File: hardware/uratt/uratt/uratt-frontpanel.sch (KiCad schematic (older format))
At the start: 25 parts, among them J9 Conn_01x10, P1 TOUCH, Q3 DMP31D0U, Q4 2N7002, SW3 SW_Push (OPTION)

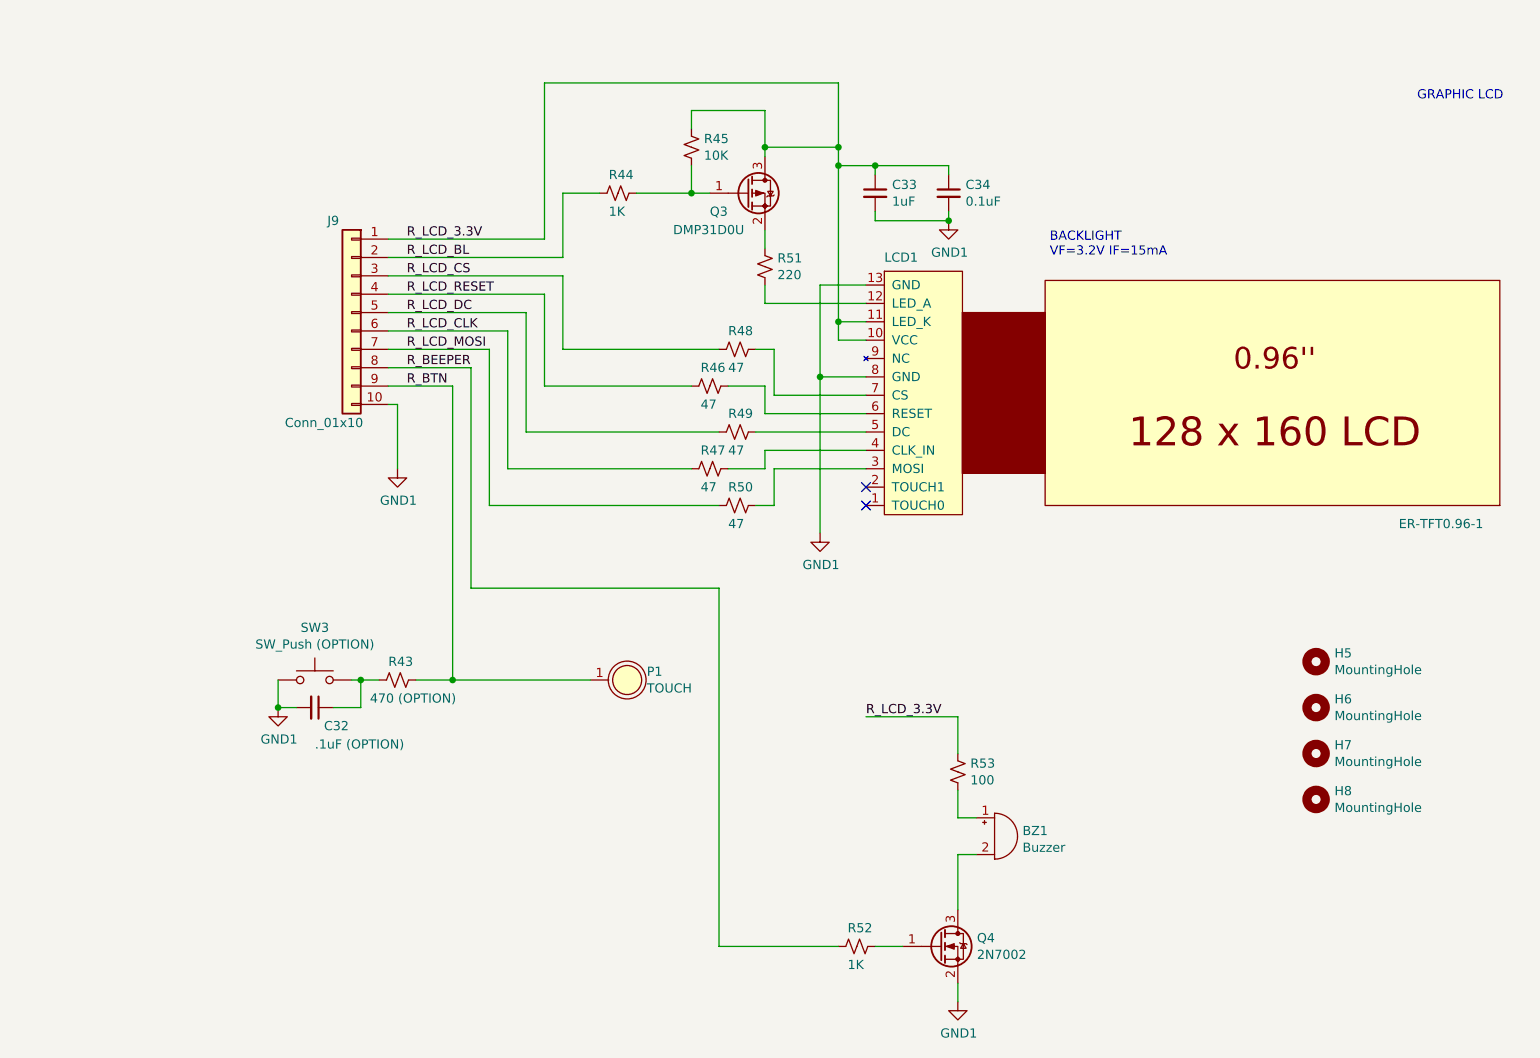
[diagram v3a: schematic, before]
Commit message: fully routed, DRC'd, outlined w/breakaways, pending final review
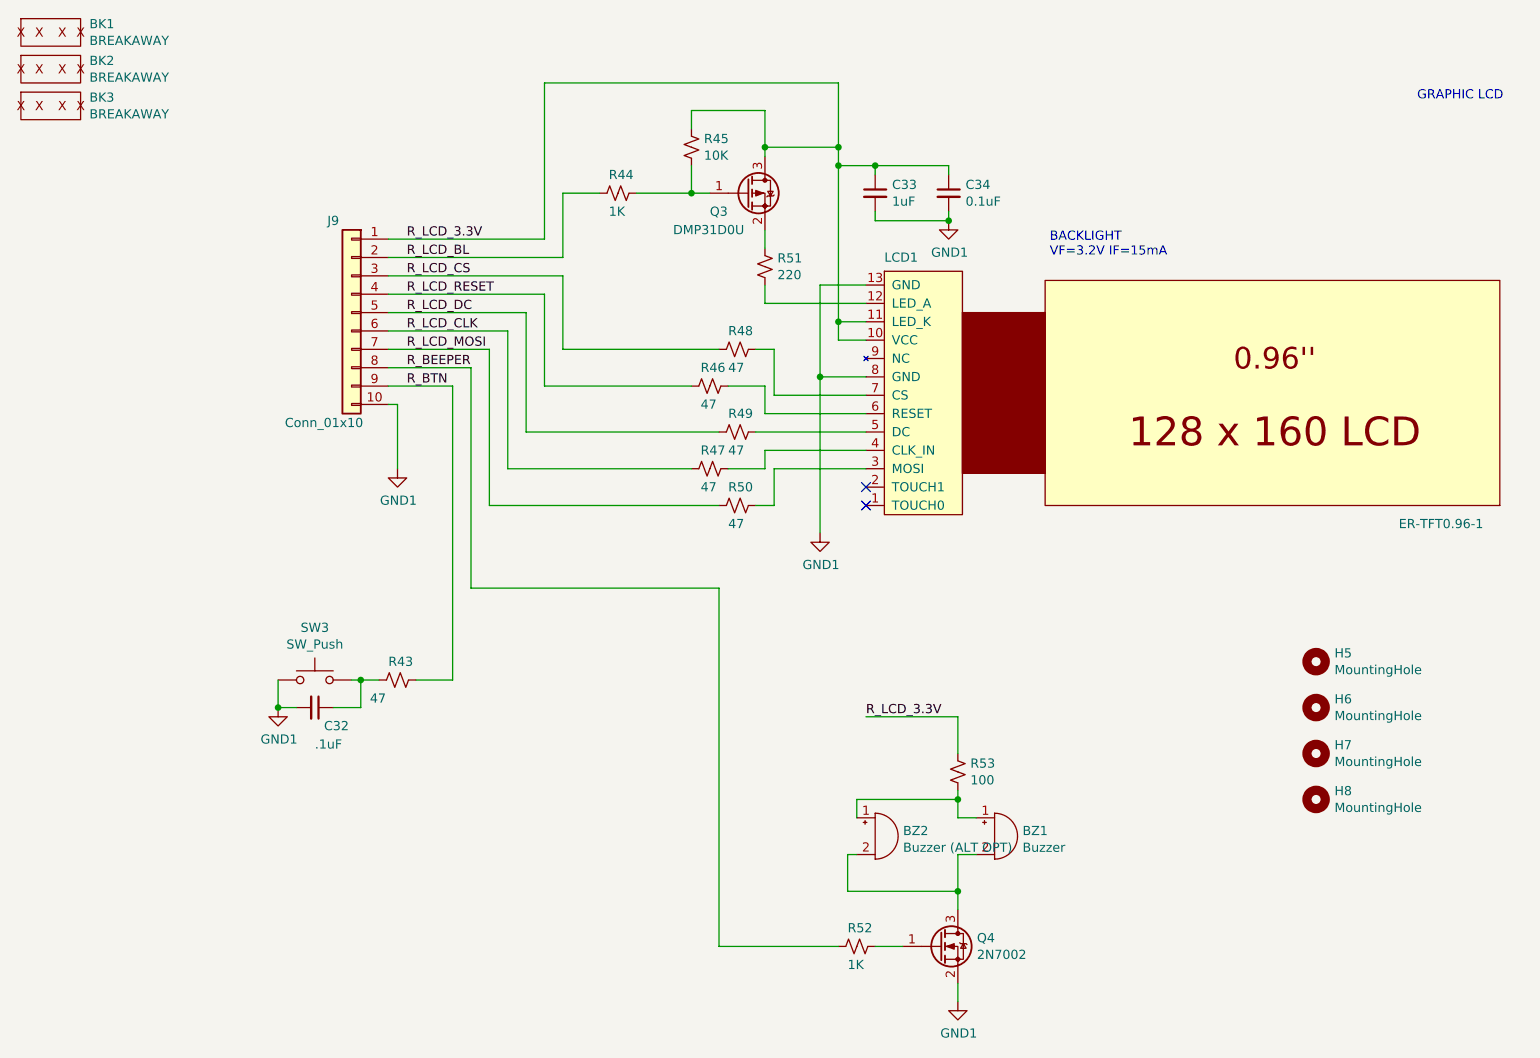
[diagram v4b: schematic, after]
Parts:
- removed P1: TOUCH, TestPoint:TestPoint_Pad_4.0x4.0mm, symbol uratt:TOUCH
- added BK1, BK2, BK3: BREAKAWAY, uratt:RATT_BITE, symbol uratt:BREAKAWAY
- added BZ2: Buzzer (ALT OPT), Buzzer_Beeper:Buzzer_CUI_CPT-9019S-SMT, symbol Device:Buzzer
- C32: value .1uF (OPTION) -> .1uF
- H5, H6, H7, H8: footprint MountingHole:MountingHole_2.7mm_M2.5 -> MountingHole:MountingHole_2.1mm
- R43: value 470 (OPTION) -> 47
- SW3: value SW_Push (OPTION) -> SW_Push
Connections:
- net at BZ1.1 (-), R53.2: now also BZ2.1 (-)
- net at BZ1.2 (+), Q4.3 (D): now also BZ2.2 (+)
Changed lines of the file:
@@
 Wire Wire Line
 	3450 3050 3450 4650
-Wire Wire Line
-	3450 4650 4200 4650
-$Comp
-L uratt:TOUCH P1
-U 1 1 631920D9
-P 4400 4650
-F 0 "P1" H 4507 4696 50  0000 L CNN
-F 1 "TOUCH" H 4507 4605 50  0000 L CNN
-F 2 "TestPoint:TestPoint_Pad_4.0x4.0mm" H 4400 4650 50  0001 C CNN
-F 3 "" H 4400 4650 50  0001 C CNN
-	1    4400 4650
-	1    0    0    -1
-$EndComp
 Connection ~ 2950 4650
 Wire Wire Line
@@
 AR Path="/62EF036B/6319A3AD" Ref="R43"  Part="1"
 F 0 "R43" V 3050 4600 50  0000 L CNN
-F 1 "470 (OPTION)" V 3250 4500 50  0000 L CNN
+F 1 "47" V 3250 4500 50  0000 L CNN
 F 2 "Resistor_SMD:R_0603_1608Metric" H 3150 4650 50  0001 C CNN
 F 3 "~" H 3150 4650 50  0001 C CNN
@@
 AR Path="/62EF036B/6319A3BE" Ref="C32"  Part="1"
 F 0 "C32" V 2800 4850 50  0000 L CNN
-F 1 ".1uF (OPTION)" V 2900 4800 50  0000 L CNN
+F 1 ".1uF" V 2900 4800 50  0000 L CNN
 F 2 "Capacitor_SMD:C_0603_1608Metric" H 2700 4800 50  0001 C CNN
 F 3 "~" H 2700 4800 50  0001 C CNN
@@
 AR Path="/62EF036B/6319A3C4" Ref="SW3"  Part="1"
 F 0 "SW3" H 2700 4935 50  0000 C CNN
-F 1 "SW_Push (OPTION)" H 2700 4844 50  0000 C CNN
+F 1 "SW_Push" H 2700 4844 50  0000 C CNN
 F 2 "Button_Switch_SMD:SW_Push_1P1T_NO_CK_KMR2" H 2700 4850 50  0001 C CNN
 F 3 "~" H 2700 4850 50  0001 C CNN
@@
 Wire Wire Line
 	3250 4650 3450 4650
-Connection ~ 3450 4650
 Text Label 3200 3050 0    50   ~ 0
 R_BTN
@@
 	6300 5400 6200 5400
 Wire Wire Line
-	6200 5400 6200 5250
+	6200 5400 6200 5300
 $Comp
 L Transistor_FET:2N7002 Q?
@@
 $EndComp
 Wire Wire Line
-	6200 5900 6200 5600
+	6200 5900 6200 5800
 Wire Wire Line
 	6200 5600 6300 5600
@@
 F 0 "H5" H 8250 4596 50  0000 L CNN
 F 1 "MountingHole" H 8250 4505 50  0000 L CNN
-F 2 "MountingHole:MountingHole_2.7mm_M2.5" H 8150 4550 50  0001 C CNN
+F 2 "MountingHole:MountingHole_2.1mm" H 8150 4550 50  0001 C CNN
 F 3 "~" H 8150 4550 50  0001 C CNN
 	1    8150 4550
@@
 F 0 "H6" H 8250 4846 50  0000 L CNN
 F 1 "MountingHole" H 8250 4755 50  0000 L CNN
-F 2 "MountingHole:MountingHole_2.7mm_M2.5" H 8150 4800 50  0001 C CNN
+F 2 "MountingHole:MountingHole_2.1mm" H 8150 4800 50  0001 C CNN
 F 3 "~" H 8150 4800 50  0001 C CNN
 	1    8150 4800
@@
 F 0 "H7" H 8250 5096 50  0000 L CNN
 F 1 "MountingHole" H 8250 5005 50  0000 L CNN
-F 2 "MountingHole:MountingHole_2.7mm_M2.5" H 8150 5050 50  0001 C CNN
+F 2 "MountingHole:MountingHole_2.1mm" H 8150 5050 50  0001 C CNN
 F 3 "~" H 8150 5050 50  0001 C CNN
 	1    8150 5050
@@
 F 0 "H8" H 8250 5346 50  0000 L CNN
 F 1 "MountingHole" H 8250 5255 50  0000 L CNN
-F 2 "MountingHole:MountingHole_2.7mm_M2.5" H 8150 5300 50  0001 C CNN
+F 2 "MountingHole:MountingHole_2.1mm" H 8150 5300 50  0001 C CNN
 F 3 "~" H 8150 5300 50  0001 C CNN
 	1    8150 5300
 	1    0    0    -1
 $EndComp
+$Comp
+L uratt:BREAKAWAY BK1
+U 1 1 5FF4E008
+P 1100 1050
+F 0 "BK1" H 1473 1021 50  0000 L CNN
+F 1 "BREAKAWAY" H 1473 930 50  0000 L CNN
+F 2 "uratt:RATT_BITE" H 1100 1050 50  0001 C CNN
+F 3 "" H 1100 1050 50  0001 C CNN
+	1    1100 1050
+	1    0    0    -1
+$EndComp
+$Comp
+L uratt:BREAKAWAY BK2
+U 1 1 5FF4E66A
+P 1100 1250
+F 0 "BK2" H 1473 1221 50  0000 L CNN
+F 1 "BREAKAWAY" H 1473 1130 50  0000 L CNN
+F 2 "uratt:RATT_BITE" H 1100 1250 50  0001 C CNN
+F 3 "" H 1100 1250 50  0001 C CNN
+	1    1100 1250
+	1    0    0    -1
+$EndComp
+$Comp
+L uratt:BREAKAWAY BK3
+U 1 1 5FF50D6B
+P 1100 1450
+F 0 "BK3" H 1473 1421 50  0000 L CNN
+F 1 "BREAKAWAY" H 1473 1330 50  0000 L CNN
+F 2 "uratt:RATT_BITE" H 1100 1450 50  0001 C CNN
+F 3 "" H 1100 1450 50  0001 C CNN
+	1    1100 1450
+	1    0    0    -1
+$EndComp
+$Comp
+L Device:Buzzer BZ?
+U 1 1 5FF0EFC7
+P 5750 5500
+AR Path="/5FF0EFC7" Ref="BZ?"  Part="1"
+AR Path="/62EF036B/5FF0EFC7" Ref="BZ2"  Part="1"
+F 0 "BZ2" H 5902 5529 50  0000 L CNN
+F 1 "Buzzer (ALT OPT)" H 5902 5438 50  0000 L CNN
+F 2 "Buzzer_Beeper:Buzzer_CUI_CPT-9019S-SMT" V 5725 5600 50  0001 C CNN
+F 3 "~" V 5725 5600 50  0001 C CNN
+	1    5750 5500
+	1    0    0    -1
+$EndComp
+Wire Wire Line
+	5650 5600 5600 5600
+Wire Wire Line
+	5600 5600 5600 5800
+Wire Wire Line
+	5600 5800 6200 5800
+Connection ~ 6200 5800
+Wire Wire Line
+	6200 5800 6200 5600
+Wire Wire Line
+	5650 5400 5650 5300
+Wire Wire Line
+	5650 5300 6200 5300
+Connection ~ 6200 5300
+Wire Wire Line
+	6200 5300 6200 5250
 $EndSCHEMATC

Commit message: add wire passthru slot, move & finalize flat flex, bigger fp button, 10V option for motor, exp connector now Grove with I2C option
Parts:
- SW3: footprint Button_Switch_SMD:SW_Push_1P1T_NO_CK_KMR2 -> Button_Switch_SMD:SW_Push_1P1T_NO_CK_KSC6xxJ
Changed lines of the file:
@@
 F 0 "SW3" H 2700 4935 50  0000 C CNN
 F 1 "SW_Push" H 2700 4844 50  0000 C CNN
-F 2 "Button_Switch_SMD:SW_Push_1P1T_NO_CK_KMR2" H 2700 4850 50  0001 C CNN
+F 2 "Button_Switch_SMD:SW_Push_1P1T_NO_CK_KSC6xxJ" H 2700 4850 50  0001 C CNN
 F 3 "~" H 2700 4850 50  0001 C CNN
 	1    2700 4650

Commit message: completed BOM, 3D STEP export
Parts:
- BK1, BK2, BK3, H5, H6, H7, H8, LCD1: Digikey (none) -> N/A
- BZ1, BZ2: Digikey (none) -> 102-3761-1-ND
- C32: value .1uF -> 0.1uF; Digikey (none) -> 732-7939-1-ND
- C33: Digikey (none) -> 587-2834-1-ND
- C34: Digikey (none) -> 732-7939-1-ND
- J9: Alt MFR Part (none) -> ZF5S-10-01-T-WT-TR; Digikey (none) -> A100293CT-ND
- Q3: Digikey (none) -> DMP31D0U-7DICT-ND
- Q4: Digikey (none) -> 2N7002Q-7-FDICT-ND
- R43, R46, R47, R48, R49, R50: Digikey (none) -> 13-RT0603FRE0747RLCT-ND
- R44, R52: Digikey (none) -> 13-RE0603FRE071KLCT-ND
- R45: Digikey (none) -> YAG2321CT-ND
- R51: Digikey (none) -> YAG5947CT-ND
- R53: Digikey (none) -> 13-RE0603FRE07100RLCT-ND
- SW3: Digikey (none) -> 401-1910-1-ND
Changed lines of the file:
@@
 F 2 "uratt:ER-TFT0.96-1" H 5750 2375 50  0001 C CNN
 F 3 "https://www.buydisplay.com/download/manual/ER-TFT0.96-1_Datasheet.pdf" H 5750 2375 50  0001 C CNN
+F 4 "N/A" H 5800 2300 50  0001 C CNN "Digikey"
 	1    5800 2300
 	1    0    0    -1
@@
 F 2 "Capacitor_SMD:C_0603_1608Metric" H 6150 2000 50  0001 C CNN
 F 3 "~" H 6150 2000 50  0001 C CNN
+F 4 "732-7939-1-ND " H 6150 2000 50  0001 C CNN "Digikey"
 	1    6150 2000
 	1    0    0    -1
@@
 F 1 "1uF" H 5842 1955 50  0000 L CNN
 F 2 "Capacitor_SMD:C_0603_1608Metric" H 5750 2000 50  0001 C CNN
-F 3 "~" H 5750 2000 50  0001 C CNN
+F 3 "http://www.yuden.co.jp/productdata/catalog/mlcc06_e.pdf" H 5750 2000 50  0001 C CNN
+F 4 "587-2834-1-ND" H 5750 2000 50  0001 C CNN "Digikey"
 	1    5750 2000
 	1    0    0    -1
@@
 F 1 "DMP31D0U" H 4650 1800 50  0000 L CNN
 F 2 "Package_TO_SOT_SMD:SOT-23" H 5250 1925 50  0001 L CIN
-F 3 "http://www.farnell.com/datasheets/1835997.pdf" H 5050 2000 50  0001 L CNN
+F 3 "https://www.diodes.com/assets/Datasheets/DMP31D0U.pdf" H 5050 2000 50  0001 L CNN
+F 4 "DMP31D0U-7DICT-ND" H 5050 2000 50  0001 C CNN "Digikey"
 	1    5050 2000
 	1    0    0    -1
@@
 F 2 "Resistor_SMD:R_0603_1608Metric" H 5150 2400 50  0001 C CNN
 F 3 "~" H 5150 2400 50  0001 C CNN
+F 4 "YAG5947CT-ND" H 5150 2400 50  0001 C CNN "Digikey"
 	1    5150 2400
 	1    0    0    -1
@@
 F 2 "Resistor_SMD:R_0603_1608Metric" H 4750 1750 50  0001 C CNN
 F 3 "~" H 4750 1750 50  0001 C CNN
+F 4 "YAG2321CT-ND" H 4750 1750 50  0001 C CNN "Digikey"
 	1    4750 1750
 	1    0    0    -1
@@
 F 2 "Resistor_SMD:R_0603_1608Metric" H 5000 2850 50  0001 C CNN
 F 3 "~" H 5000 2850 50  0001 C CNN
+F 4 "13-RT0603FRE0747RLCT-ND" H 5000 2850 50  0001 C CNN "Digikey"
 	1    5000 2850
 	0    1    1    0
@@
 F 2 "Resistor_SMD:R_0603_1608Metric" H 4850 3050 50  0001 C CNN
 F 3 "~" H 4850 3050 50  0001 C CNN
+F 4 "13-RT0603FRE0747RLCT-ND" H 4850 3050 50  0001 C CNN "Digikey"
 	1    4850 3050
 	0    1    1    0
@@
 F 2 "Resistor_SMD:R_0603_1608Metric" H 5000 3300 50  0001 C CNN
 F 3 "~" H 5000 3300 50  0001 C CNN
+F 4 "13-RT0603FRE0747RLCT-ND" H 5000 3300 50  0001 C CNN "Digikey"
 	1    5000 3300
 	0    1    1    0
@@
 F 2 "Resistor_SMD:R_0603_1608Metric" H 4850 3500 50  0001 C CNN
 F 3 "~" H 4850 3500 50  0001 C CNN
+F 4 "13-RT0603FRE0747RLCT-ND" H 4850 3500 50  0001 C CNN "Digikey"
 	1    4850 3500
 	0    1    1    0
@@
 F 2 "Resistor_SMD:R_0603_1608Metric" H 5000 3700 50  0001 C CNN
 F 3 "~" H 5000 3700 50  0001 C CNN
+F 4 "13-RT0603FRE0747RLCT-ND" H 5000 3700 50  0001 C CNN "Digikey"
 	1    5000 3700
 	0    1    1    0
@@
 F 2 "Resistor_SMD:R_0603_1608Metric" H 4350 2000 50  0001 C CNN
 F 3 "~" H 4350 2000 50  0001 C CNN
+F 4 "13-RE0603FRE071KLCT-ND" H 4350 2000 50  0001 C CNN "Digikey"
 	1    4350 2000
 	0    1    1    0
@@
 F 1 "Conn_01x10" H 3050 2050 50  0000 C CNN
 F 2 "Connector_FFC-FPC:TE_1-1734839-0_1x10-1MP_P0.5mm_Horizontal" H 2900 2650 50  0001 C CNN
-F 3 "~" H 2900 2650 50  0001 C CNN
+F 3 "https://www.te.com/commerce/DocumentDelivery/DDEController?Action=srchrtrv&DocNm=1734839&DocType=Customer+Drawing&DocLang=English" H 2900 2650 50  0001 C CNN
+F 4 "" H 2900 2650 50  0001 C CNN "Field4"
+F 5 "ZF5S-10-01-T-WT-TR" H 2900 2650 50  0001 C CNN "Alt MFR Part"
+F 6 "A100293CT-ND" H 2900 2650 50  0001 C CNN "Digikey"
 	1    2900 2650
 	-1   0    0    -1
@@
 F 2 "Resistor_SMD:R_0603_1608Metric" H 3150 4650 50  0001 C CNN
 F 3 "~" H 3150 4650 50  0001 C CNN
+F 4 "13-RT0603FRE0747RLCT-ND" H 3150 4650 50  0001 C CNN "Digikey"
 	1    3150 4650
 	0    1    1    0
@@
 AR Path="/62EF036B/6319A3BE" Ref="C32"  Part="1"
 F 0 "C32" V 2800 4850 50  0000 L CNN
-F 1 ".1uF" V 2900 4800 50  0000 L CNN
+F 1 "0.1uF" V 2900 4800 50  0000 L CNN
 F 2 "Capacitor_SMD:C_0603_1608Metric" H 2700 4800 50  0001 C CNN
 F 3 "~" H 2700 4800 50  0001 C CNN
+F 4 "732-7939-1-ND " H 2700 4800 50  0001 C CNN "Digikey"
 	1    2700 4800
 	0    1    1    0
@@
 F 1 "SW_Push" H 2700 4844 50  0000 C CNN
 F 2 "Button_Switch_SMD:SW_Push_1P1T_NO_CK_KSC6xxJ" H 2700 4850 50  0001 C CNN
-F 3 "~" H 2700 4850 50  0001 C CNN
+F 3 "https://www.ckswitches.com/media/1973/ksc7.pdf" H 2700 4850 50  0001 C CNN
+F 4 "" H 2700 4650 50  0001 C CNN "Field4"
+F 5 "	401-1910-1-ND" H 2700 4650 50  0001 C CNN "Digikey"
 	1    2700 4650
 	1    0    0    -1
@@
 F 1 "Buzzer" H 6552 5438 50  0000 L CNN
 F 2 "Buzzer_Beeper:Buzzer_CUI_CPT-9019S-SMT" V 6375 5600 50  0001 C CNN
-F 3 "~" V 6375 5600 50  0001 C CNN
+F 3 "https://www.cuidevices.com/product/resource/cpt-9019s-smt-tr.pdf" V 6375 5600 50  0001 C CNN
+F 4 "" H 6400 5500 50  0001 C CNN "Field4"
+F 5 "102-3761-1-ND" H 6400 5500 50  0001 C CNN "Digikey"
 	1    6400 5500
 	1    0    0    -1
@@
 F 1 "2N7002" H 6304 6055 50  0000 L CNN
 F 2 "Package_TO_SOT_SMD:SOT-23" H 6300 6025 50  0001 L CIN
-F 3 "https://www.onsemi.com/pub/Collateral/NDS7002A-D.PDF" H 6100 6100 50  0001 L CNN
+F 3 "https://www.diodes.com/assets/Datasheets/2N7002.pdf" H 6100 6100 50  0001 L CNN
+F 4 "2N7002Q-7-FDICT-ND" H 6100 6100 50  0001 C CNN "Digikey"
 	1    6100 6100
 	1    0    0    -1
@@
 F 2 "Resistor_SMD:R_0603_1608Metric" H 6200 5150 50  0001 C CNN
 F 3 "~" H 6200 5150 50  0001 C CNN
+F 4 "13-RE0603FRE07100RLCT-ND" H 6200 5150 50  0001 C CNN "Digikey"
 	1    6200 5150
 	1    0    0    -1
@@
 F 2 "Resistor_SMD:R_0603_1608Metric" H 5650 6100 50  0001 C CNN
 F 3 "~" H 5650 6100 50  0001 C CNN
+F 4 "13-RE0603FRE071KLCT-ND" H 5650 6100 50  0001 C CNN "Digikey"
 	1    5650 6100
 	0    1    1    0
@@
 F 2 "MountingHole:MountingHole_2.1mm" H 8150 4550 50  0001 C CNN
 F 3 "~" H 8150 4550 50  0001 C CNN
+F 4 "N/A" H 8150 4550 50  0001 C CNN "Digikey"
 	1    8150 4550
 	1    0    0    -1
@@
 F 2 "MountingHole:MountingHole_2.1mm" H 8150 4800 50  0001 C CNN
 F 3 "~" H 8150 4800 50  0001 C CNN
+F 4 "N/A" H 8150 4800 50  0001 C CNN "Digikey"
 	1    8150 4800
 	1    0    0    -1
@@
 F 2 "MountingHole:MountingHole_2.1mm" H 8150 5050 50  0001 C CNN
 F 3 "~" H 8150 5050 50  0001 C CNN
+F 4 "N/A" H 8150 5050 50  0001 C CNN "Digikey"
 	1    8150 5050
 	1    0    0    -1
@@
 F 2 "MountingHole:MountingHole_2.1mm" H 8150 5300 50  0001 C CNN
 F 3 "~" H 8150 5300 50  0001 C CNN
+F 4 "N/A" H 8150 5300 50  0001 C CNN "Digikey"
 	1    8150 5300
 	1    0    0    -1
@@
 F 2 "uratt:RATT_BITE" H 1100 1050 50  0001 C CNN
 F 3 "" H 1100 1050 50  0001 C CNN
+F 4 "N/A" H 1100 1050 50  0001 C CNN "Digikey"
 	1    1100 1050
 	1    0    0    -1
@@
 F 2 "uratt:RATT_BITE" H 1100 1250 50  0001 C CNN
 F 3 "" H 1100 1250 50  0001 C CNN
+F 4 "N/A" H 1100 1250 50  0001 C CNN "Digikey"
 	1    1100 1250
 	1    0    0    -1
@@
 F 2 "uratt:RATT_BITE" H 1100 1450 50  0001 C CNN
 F 3 "" H 1100 1450 50  0001 C CNN
+F 4 "N/A" H 1100 1450 50  0001 C CNN "Digikey"
 	1    1100 1450
 	1    0    0    -1
@@
 F 1 "Buzzer (ALT OPT)" H 5902 5438 50  0000 L CNN
 F 2 "Buzzer_Beeper:Buzzer_CUI_CPT-9019S-SMT" V 5725 5600 50  0001 C CNN
-F 3 "~" V 5725 5600 50  0001 C CNN
+F 3 "https://www.cuidevices.com/product/resource/cpt-9019s-smt-tr.pdf" V 5725 5600 50  0001 C CNN
+F 4 "102-3761-1-ND" H 5750 5500 50  0001 C CNN "Digikey"
 	1    5750 5500
 	1    0    0    -1
